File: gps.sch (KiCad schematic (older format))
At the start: 14 parts, among them J14 GPS, Q1 2N7002NXAK, Q2 BSH202, U3 L76

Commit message: Added images Added information to schematic Added information to layout
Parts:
- renumbered C19 to C17, C20 to C18, C21 to C19, C22 to C20, J14 to J13
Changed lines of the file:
@@
 encoding utf-8
 Sheet 7 11
-Title ""
-Date ""
-Rev ""
-Comp ""
-Comment1 ""
+Title "AirMon"
+Date "2020-01-13"
+Rev "0.1"
+Comp "Jörg Bayer"
+Comment1 "CC BY 4.0"
 Comment2 ""
 Comment3 ""
@@
 	4600 1900 4600 2500
 $Comp
-L power:VSS #PWR028
+L power:VSS #PWR027
 U 1 1 5E1BB4E8
 P 4500 4500
-F 0 "#PWR028" H 4500 4350 50  0001 C CNN
+F 0 "#PWR027" H 4500 4350 50  0001 C CNN
 F 1 "VSS" H 4400 4600 50  0000 C CNN
 F 2 "" H 4500 4500 50  0001 C CNN
@@
 	3800 3100 3600 3100
 $Comp
-L power:VCC #PWR027
+L power:VCC #PWR026
 U 1 1 5E1BB4F4
 P 4500 1800
-F 0 "#PWR027" H 4500 1650 50  0001 C CNN
+F 0 "#PWR026" H 4500 1650 50  0001 C CNN
 F 1 "VCC" H 4517 1973 50  0000 C CNN
 F 2 "" H 4500 1800 50  0001 C CNN
@@
 	6100 3300 6200 3300
 $Comp
-L Connector_Generic:Conn_01x02 J14
+L Connector_Generic:Conn_01x02 J13
 U 1 1 5E1BB52C
 P 6300 3500
-F 0 "J14" H 6379 3492 50  0000 L CNN
+F 0 "J13" H 6379 3492 50  0000 L CNN
 F 1 "GPS" H 6379 3401 50  0000 L CNN
 F 2 "Connector_Coaxial:U.FL_Molex_MCRF_73412-0110_Vertical" H 6300 3500 50  0001 C CNN
@@
 Connection ~ 5900 3900
 $Comp
-L power:VSS #PWR029
+L power:VSS #PWR028
 U 1 1 5E1BB568
 P 5900 3900
-F 0 "#PWR029" H 5900 3750 50  0001 C CNN
+F 0 "#PWR028" H 5900 3750 50  0001 C CNN
 F 1 "VSS" H 5800 4000 50  0000 C CNN
 F 2 "" H 5900 3900 50  0001 C CNN
@@
 AR Path="/5E151517/5E29A65B" Ref="C?"  Part="1"
 AR Path="/5E1991ED/5E29A65B" Ref="C?"  Part="1"
-AR Path="/5E1BB661/5E29A65B" Ref="C21"  Part="1"
-F 0 "C21" H 3715 2196 50  0000 L CNN
+AR Path="/5E1BB661/5E29A65B" Ref="C19"  Part="1"
+F 0 "C19" H 3715 2196 50  0000 L CNN
 F 1 "1u" H 3715 2105 50  0000 L CNN
 F 2 "Capacitor_SMD:C_0805_2012Metric" H 3638 2000 50  0001 C CNN
@@
 	3600 2300 3600 2400
 $Comp
-L power:VSS #PWR026
+L power:VSS #PWR025
 U 1 1 5E29E1E1
 P 3600 2500
-F 0 "#PWR026" H 3600 2350 50  0001 C CNN
+F 0 "#PWR025" H 3600 2350 50  0001 C CNN
 F 1 "VSS" H 3500 2600 50  0000 C CNN
 F 2 "" H 3600 2500 50  0001 C CNN
@@
 AR Path="/5E15DEC3/5E2A1D19" Ref="C?"  Part="1"
 AR Path="/5E151517/5E2A1D19" Ref="C?"  Part="1"
-AR Path="/5E1BB661/5E2A1D19" Ref="C22"  Part="1"
-F 0 "C22" H 4115 2196 50  0000 L CNN
+AR Path="/5E1BB661/5E2A1D19" Ref="C20"  Part="1"
+F 0 "C20" H 4115 2196 50  0000 L CNN
 F 1 "100n" H 4115 2105 50  0000 L CNN
 F 2 "Capacitor_SMD:C_0603_1608Metric" H 4038 2000 50  0001 C CNN
@@
 AR Path="/5E151517/5E2A54E4" Ref="C?"  Part="1"
 AR Path="/5E1991ED/5E2A54E4" Ref="C?"  Part="1"
-AR Path="/5E1BB661/5E2A54E4" Ref="C19"  Part="1"
-F 0 "C19" H 2915 2196 50  0000 L CNN
+AR Path="/5E1BB661/5E2A54E4" Ref="C17"  Part="1"
+F 0 "C17" H 2915 2196 50  0000 L CNN
 F 1 "1u" H 2915 2105 50  0000 L CNN
 F 2 "Capacitor_SMD:C_0805_2012Metric" H 2838 2000 50  0001 C CNN
@@
 AR Path="/5E15DEC3/5E2A54EC" Ref="C?"  Part="1"
 AR Path="/5E151517/5E2A54EC" Ref="C?"  Part="1"
-AR Path="/5E1BB661/5E2A54EC" Ref="C20"  Part="1"
-F 0 "C20" H 3315 2196 50  0000 L CNN
+AR Path="/5E1BB661/5E2A54EC" Ref="C18"  Part="1"
+F 0 "C18" H 3315 2196 50  0000 L CNN
 F 1 "100n" H 3315 2105 50  0000 L CNN
 F 2 "Capacitor_SMD:C_0603_1608Metric" H 3238 2000 50  0001 C CNN

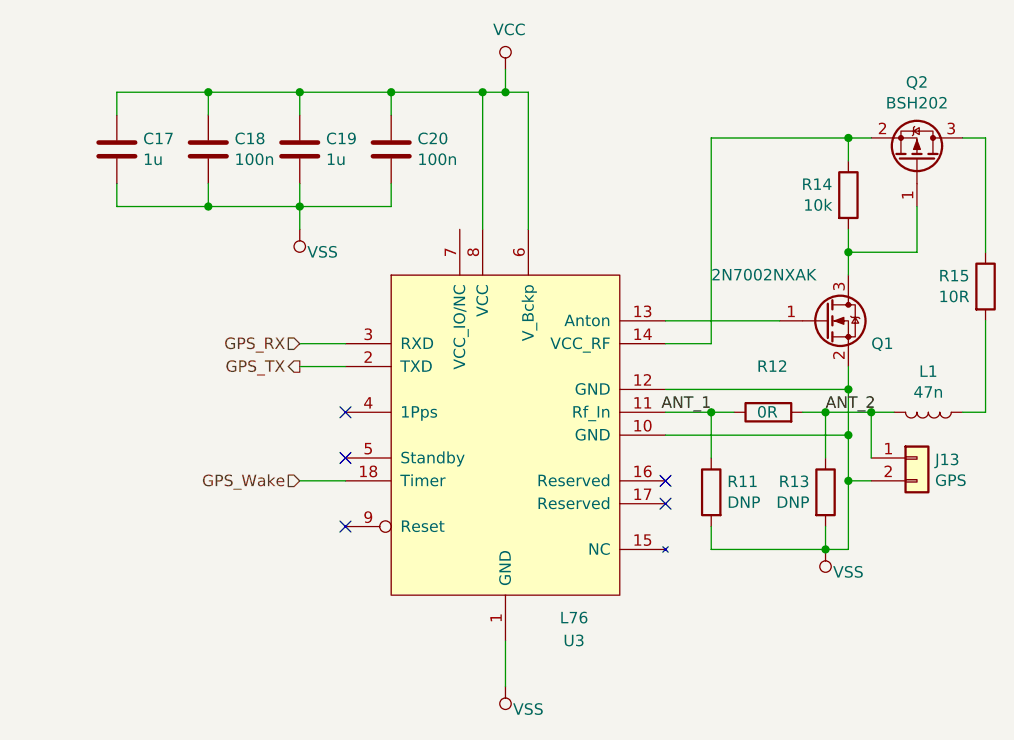
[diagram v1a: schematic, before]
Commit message: Added Readme Added GNSS receiver list Fixed GNSS receiver connections Improved Pictures
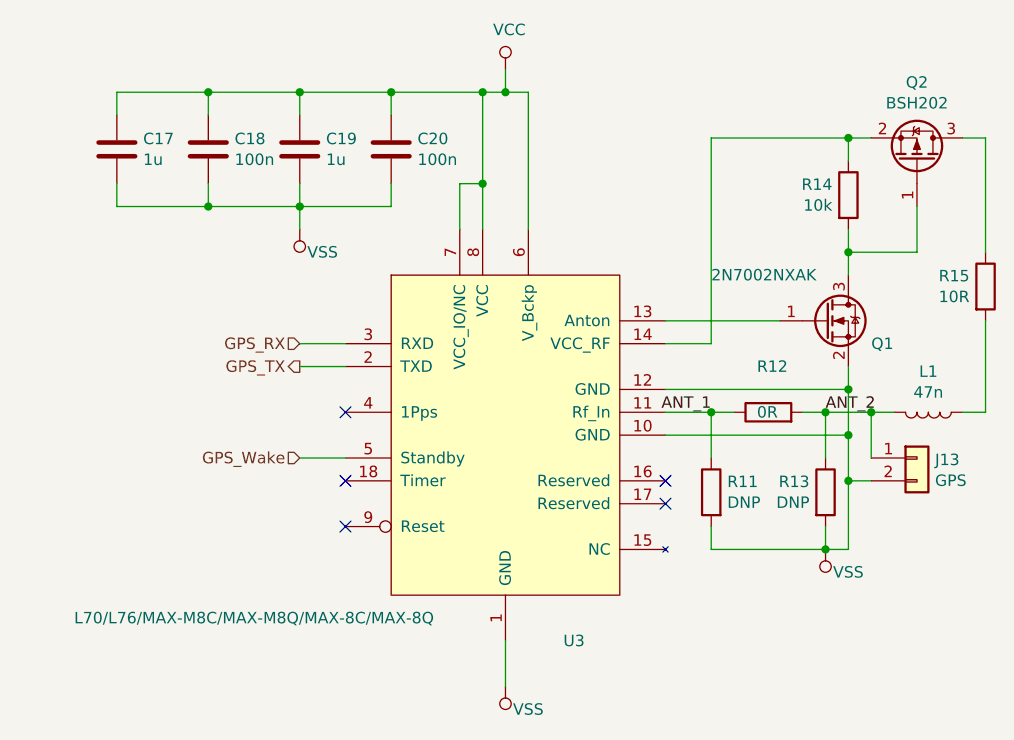
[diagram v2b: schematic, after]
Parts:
- U3: value L76 -> L70/L76/MAX-M8C/MAX-M8Q/MAX-8C/MAX-8Q
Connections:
- net GPS_Wake: now also U3.5 (Standby); no longer U3.18 (Timer)
- net VCC: now also U3.7 (VCC_IO/NC)
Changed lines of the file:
@@
 P 4500 3400
 F 0 "U3" H 4800 2500 50  0000 C CNN
-F 1 "L76" H 4800 2600 50  0000 C CNN
+F 1 "L70/L76/MAX-M8C/MAX-M8Q/MAX-8C/MAX-8Q" H 3400 2600 50  0000 C CNN
 F 2 "global:L70" H 4100 3500 50  0001 C CNN
 F 3 "https://www.quectel.com/UploadImage/Downlad/L70_Hardware_Design_V2.0.pdf" H 4100 3500 50  0001 C CNN
@@
 $EndComp
 NoConn ~ 3800 3300
-NoConn ~ 3800 3500
+NoConn ~ 3800 3600
 NoConn ~ 5200 3600
 NoConn ~ 5200 3700
@@
 	4500 4300 4500 4500
 Wire Wire Line
-	4400 2500 4400 1900
+	4400 2500 4400 2300
 Wire Wire Line
 	4400 1900 4500 1900
@@
 $EndComp
 Wire Wire Line
-	3800 3600 3600 3600
+	3800 3500 3600 3500
 Wire Wire Line
 	3800 3000 3600 3000
@@
 Text HLabel 3600 3100 0    50   Output ~ 0
 GPS_TX
-Text HLabel 3600 3600 0    50   Input ~ 0
+Text HLabel 3600 3500 0    50   Input ~ 0
 GPS_Wake
 $Comp
@@
 Wire Wire Line
 	6000 3600 6000 3900
+Wire Wire Line
+	4300 2500 4300 2300
+Wire Wire Line
+	4300 2300 4400 2300
+Connection ~ 4400 2300
+Wire Wire Line
+	4400 2300 4400 1900
 $EndSCHEMATC

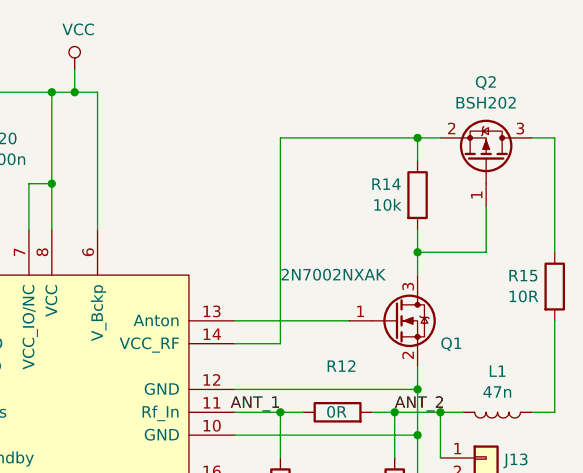
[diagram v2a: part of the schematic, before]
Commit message: Added fuse for USB Added buttons for boot and reset Added version number to PCB Changed several component values for improved manufacturing Added BOM Added component position file
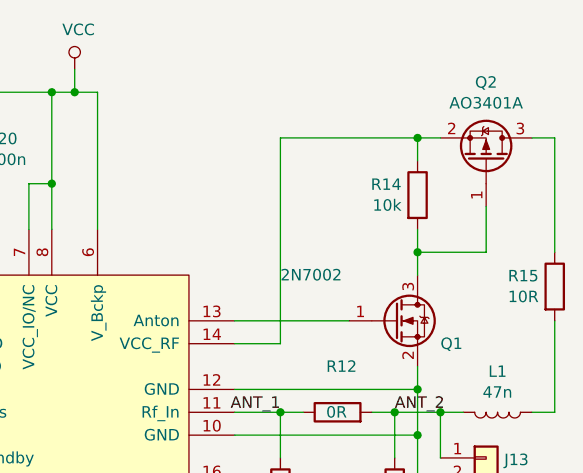
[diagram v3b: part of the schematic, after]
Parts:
- C17, C19: lcsc# (none) -> C28323; manf# CL21B105KBFNNNG -> CL21B105KBFNNNE
- C18, C20: lcsc# (none) -> C14663; manf# CL10B104KB8NNNL -> CC0603KRX7R9BB104
- J13: lcsc# (none) -> C88374; manf# (none) -> U.FL-R-SMT-1(80)
- L1: lcsc# (none) -> C29683; manf# (none) -> SDCL1608C47NJTDF
- Q1: value 2N7002NXAK -> 2N7002; lcsc# (none) -> C8545; manf# (none) -> 2N7002
- Q2: value BSH202 -> AO3401A; lcsc# (none) -> C15127; manf# BSH202 -> AO3401A
- R12: lcsc# (none) -> C21189; manf# (none) -> 0603WAF0000T5E
- R14: lcsc# (none) -> C25804; manf# (none) -> 0603WAF1002T5E
- R15: lcsc# (none) -> C22859; manf# (none) -> 0603WAF100JT5E
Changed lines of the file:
@@
 AR Path="/5E1BB661/5E1BB4FC" Ref="Q1"  Part="1"
 F 0 "Q1" H 6100 2800 50  0000 L CNN
-F 1 "2N7002NXAK" H 5400 3100 50  0000 L CNN
+F 1 "2N7002" H 5400 3100 50  0000 L CNN
 F 2 "Package_TO_SOT_SMD:SOT-23" H 6100 3000 50  0001 C CNN
 F 3 "~" H 5900 2900 50  0001 C CNN
+F 4 "C8545" H 0   0   50  0001 C CNN "lcsc#"
+F 5 "2N7002" H 0   0   50  0001 C CNN "manf#"
 	1    5900 2900
 	1    0    0    -1
@@
 F 2 "Resistor_SMD:R_0603_1608Metric" V 5930 2350 50  0001 C CNN
 F 3 "~" H 6000 2350 50  0001 C CNN
+F 4 "C25804" H 0   0   50  0001 C CNN "lcsc#"
+F 5 "0603WAF1002T5E" H 0   0   50  0001 C CNN "manf#"
 	1    6000 2350
 	1    0    0    -1
@@
 AR Path="/5E1BB661/5E1BB50D" Ref="Q2"  Part="1"
 F 0 "Q2" V 6643 2200 50  0000 C CNN
-F 1 "BSH202" V 6552 2200 50  0000 C CNN
+F 1 "AO3401A" V 6552 2200 50  0000 C CNN
 F 2 "Package_TO_SOT_SMD:SOT-23" H 6500 2300 50  0001 C CNN
 F 3 "~" H 6300 2200 50  0001 C CNN
-F 4 "BSH202" H 6300 2200 50  0001 C CNN "manf#"
+F 4 "AO3401A" H 6300 2200 50  0001 C CNN "manf#"
+F 5 "C15127" H 0   0   50  0001 C CNN "lcsc#"
 	1    6300 2200
 	0    1    -1   0
@@
 F 2 "Inductor_SMD:L_0603_1608Metric" H 6350 3300 50  0001 C CNN
 F 3 "~" H 6350 3300 50  0001 C CNN
+F 4 "C29683" V 6350 3300 50  0001 C CNN "lcsc#"
+F 5 "SDCL1608C47NJTDF" H 0   0   50  0001 C CNN "manf#"
 	1    6350 3300
 	0    1    1    0
@@
 F 2 "Connector_Coaxial:U.FL_Molex_MCRF_73412-0110_Vertical" H 6300 3500 50  0001 C CNN
 F 3 "~" H 6300 3500 50  0001 C CNN
+F 4 "C88374" H 0   0   50  0001 C CNN "lcsc#"
+F 5 "U.FL-R-SMT-1(80)" H 0   0   50  0001 C CNN "manf#"
 	1    6300 3500
 	1    0    0    -1
@@
 F 2 "Resistor_SMD:R_0603_1608Metric" V 6530 2750 50  0001 C CNN
 F 3 "~" H 6600 2750 50  0001 C CNN
+F 4 "C22859" H 0   0   50  0001 C CNN "lcsc#"
+F 5 "0603WAF100JT5E" H 0   0   50  0001 C CNN "manf#"
 	1    6600 2750
 	1    0    0    -1
@@
 F 2 "Resistor_SMD:R_0603_1608Metric" V 5580 3300 50  0001 C CNN
 F 3 "~" H 5650 3300 50  0001 C CNN
+F 4 "C21189" H 0   0   50  0001 C CNN "lcsc#"
+F 5 "0603WAF0000T5E" H 0   0   50  0001 C CNN "manf#"
 	1    5650 3300
 	0    -1   -1   0
@@
 F 2 "Capacitor_SMD:C_0805_2012Metric" H 3638 2000 50  0001 C CNN
 F 3 "~" H 3600 2150 50  0001 C CNN
-F 4 "CL21B105KBFNNNG" H 3600 2150 50  0001 C CNN "manf#"
+F 4 "CL21B105KBFNNNE" H 3600 2150 50  0001 C CNN "manf#"
+F 5 "C28323" H 0   0   50  0001 C CNN "lcsc#"
 	1    3600 2150
 	1    0    0    -1
@@
 F 2 "Capacitor_SMD:C_0603_1608Metric" H 4038 2000 50  0001 C CNN
 F 3 "~" H 4000 2150 50  0001 C CNN
-F 4 "CL10B104KB8NNNL" H 4000 2150 50  0001 C CNN "manf#"
+F 4 "CC0603KRX7R9BB104" H 4000 2150 50  0001 C CNN "manf#"
+F 5 "C14663" H 0   0   50  0001 C CNN "lcsc#"
 	1    4000 2150
 	1    0    0    -1
@@
 F 2 "Capacitor_SMD:C_0805_2012Metric" H 2838 2000 50  0001 C CNN
 F 3 "~" H 2800 2150 50  0001 C CNN
-F 4 "CL21B105KBFNNNG" H 2800 2150 50  0001 C CNN "manf#"
+F 4 "CL21B105KBFNNNE" H 2800 2150 50  0001 C CNN "manf#"
+F 5 "C28323" H 0   0   50  0001 C CNN "lcsc#"
 	1    2800 2150
 	1    0    0    -1
@@
 F 2 "Capacitor_SMD:C_0603_1608Metric" H 3238 2000 50  0001 C CNN
 F 3 "~" H 3200 2150 50  0001 C CNN
-F 4 "CL10B104KB8NNNL" H 3200 2150 50  0001 C CNN "manf#"
+F 4 "CC0603KRX7R9BB104" H 3200 2150 50  0001 C CNN "manf#"
+F 5 "C14663" H 0   0   50  0001 C CNN "lcsc#"
 	1    3200 2150
 	1    0    0    -1
